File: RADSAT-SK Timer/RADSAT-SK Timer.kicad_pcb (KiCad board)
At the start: 2 copper layers, 90.2 x 95.9 mm, 122 parts, among them J101 Conn_02x26_Odd_Even, J103 Conn_02x26_Odd_Even, J201 Conn_01x07, J202 Conn_01x05, J203 Conn_01x03, J204 Conn_01x02, J205 Conn_01x02, J206 Conn_01x02, J210 ZX62WRD-B-5PC, Q101 IRLML2060, Q102 IRLML2060, Q103 IRLML2060, Q104 IRLML2060, Q105 IRLML2060, Q106 IRLML2060, Q107 IRLML2060, Q108 IRLML2060, Q109 IRLML2060, Q201 IRLML2060, Q202 IRLML2060, Q204 IRLML2060, Q205 IRLML2060, Q206 IRLML2060, SW201 SW_Push, SW202 SW_Push, SW203 SW_Push, SW204 SW_Push, SW205 SW_Push, SW206 SW_Push, U101 LM397MF, U102 LM397MF, U103 LM397MF, U104 CD4052B, U202 LTC3440EMSPBF, U230 CPC1117N, U240 CPC1117N, U250 CPC1117N, U260 CPC1117N

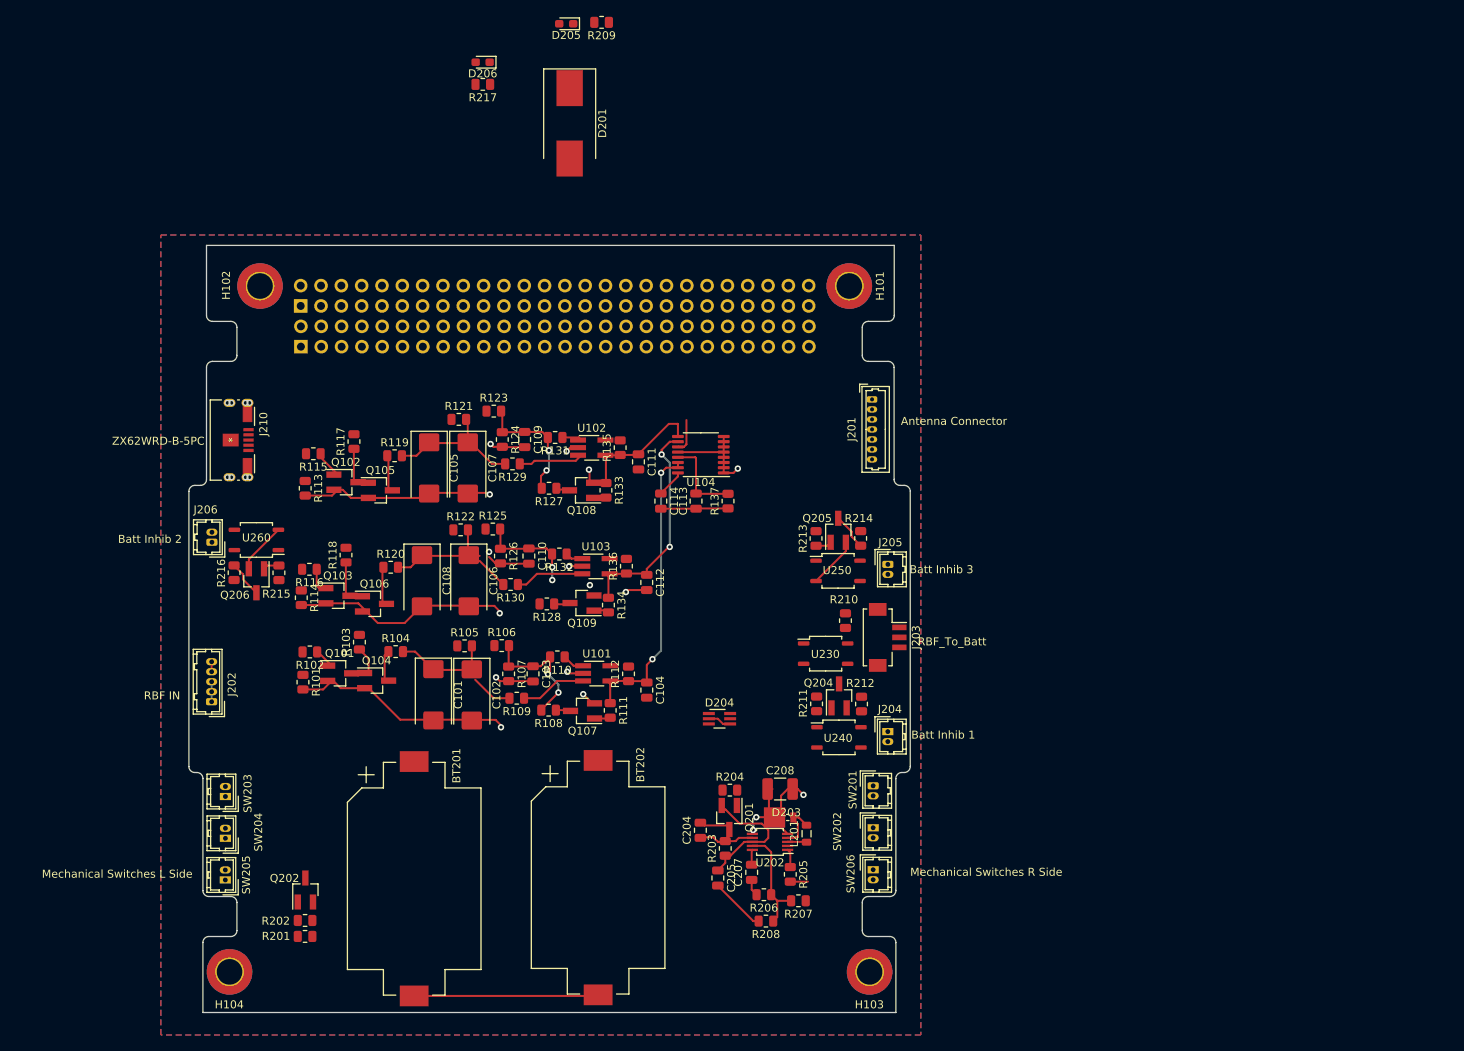
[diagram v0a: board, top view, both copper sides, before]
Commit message: better layour for timer components
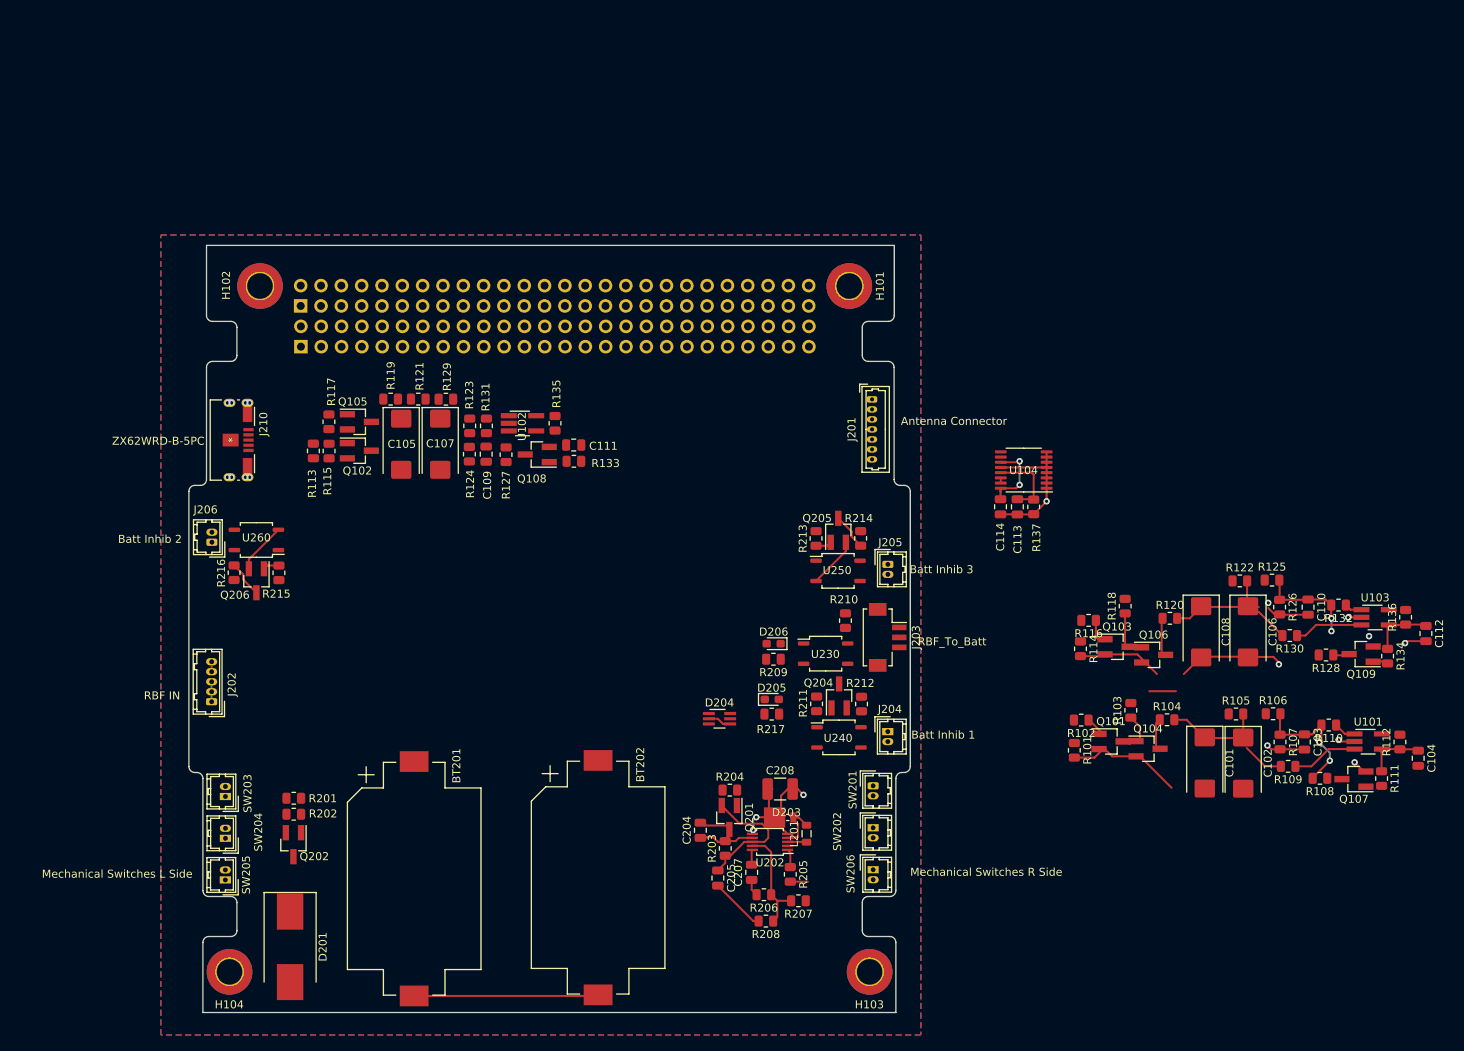
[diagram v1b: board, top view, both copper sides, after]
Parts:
- moved D201 108.7 mm to (47.5, 137.7)
- moved C108 97.6 mm to (161.4, 98.3)
- moved R120 97.6 mm to (157.5, 96.6)
- moved R122 97.6 mm to (166.2, 91.9)
- moved R134 97.6 mm to (184.7, 101.3)
- moved R136 97.6 mm to (186.9, 96.5)
- moved U103 97.6 mm to (183.1, 96.5)
- moved C106 97.6 mm to (167.2, 98.3)
- moved C110 97.6 mm to (174.7, 95.2)
- moved C112 97.6 mm to (189.5, 98.5)
- moved Q103 97.6 mm to (150.8, 100.2)
- moved Q106 97.6 mm to (155.4, 101.2)
- moved R114 97.6 mm to (146.3, 100.4)
- moved R126 97.6 mm to (171.2, 95.2)
- moved R130 97.6 mm to (172.4, 98.8)
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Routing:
- net GND: track 147.7 -> 100.2 mm, vias 15 -> 10
- net Timer_A_out: track 37.9 -> 8.59 mm, vias 2 -> 0
- net Timer_C_out: track 28.0 -> 8.28 mm, vias 2 -> 0
- net Net-(C105-Pad1): track 17.2 -> 0.00 mm
- net Timer_B_out: track 16.3 -> 0.00 mm
- net Net-(C109-Pad1): track 15.4 -> 0.00 mm, vias 2 -> 0
- net Net-(R129-Pad1): track 8.13 -> 0.00 mm
- net Net-(Q102-Pad3): track 6.52 -> 0.09 mm
- net Net-(Q105-Pad3): track 4.37 -> 0.00 mm
- net Net-(Q102-Pad1): track 3.50 -> 0.00 mm
- net Net-(Q107-Pad1): track 2.50 -> 0.00 mm
- net Net-(R131-Pad1): track 2.48 -> 0.00 mm
- net Net-(Q107-Pad3): track 2.37 -> 0.00 mm
- net Net-(Q108-Pad3): track 2.26 -> 0.00 mm
- net Net-(Q108-Pad1): track 2.06 -> 0.00 mm
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
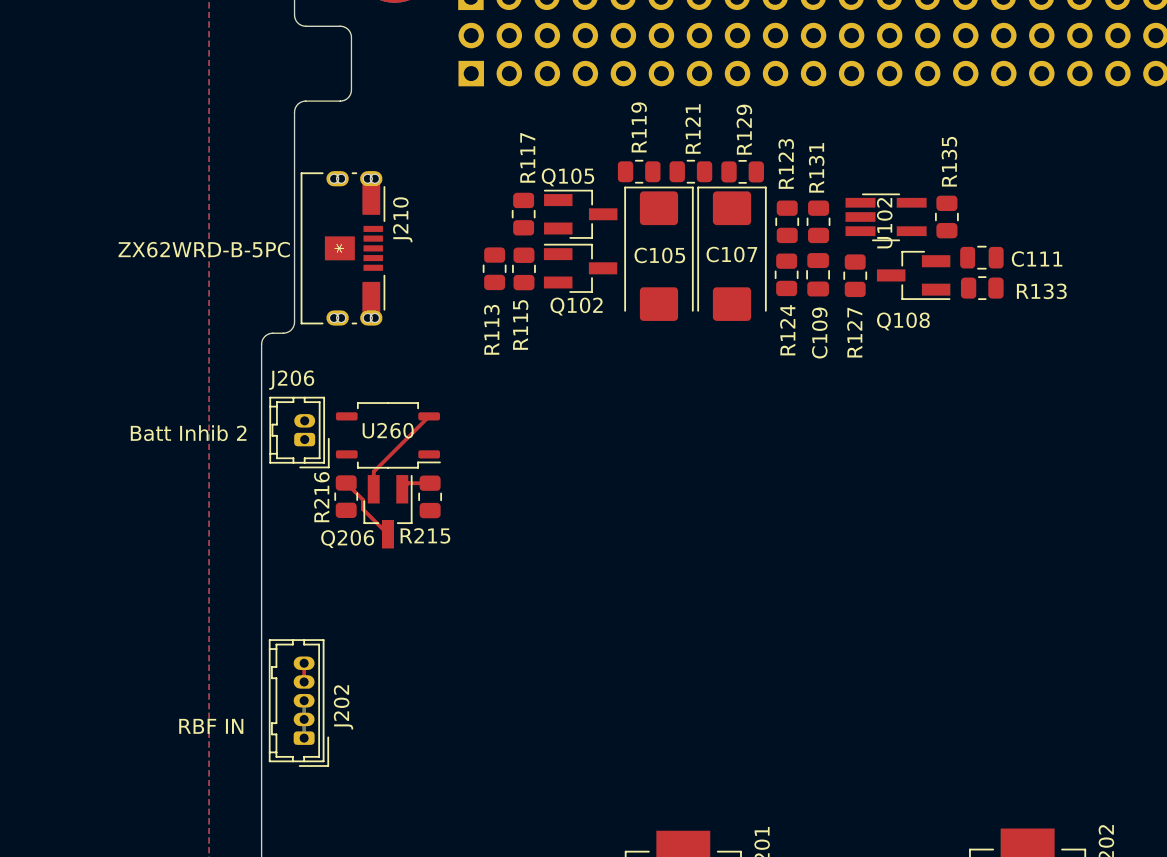
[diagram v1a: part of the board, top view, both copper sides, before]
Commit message: Made changes to accomadate the RBF alternate charge plug
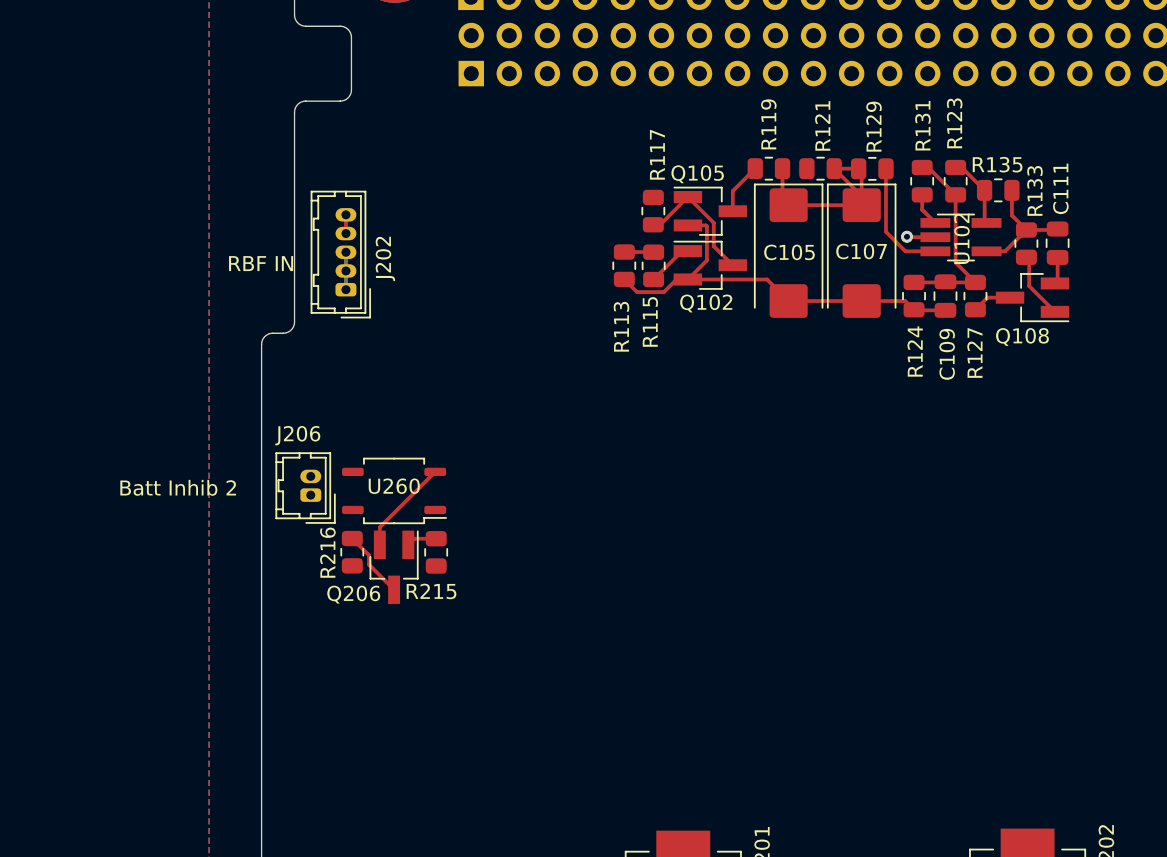
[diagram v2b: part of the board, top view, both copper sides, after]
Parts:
- removed J210: ZX62WRD-B-5PC, CONN_ZX62WRD-B-5PC_HIR:CONN_ZX62WRD-B-5PC_HIR
- moved J202 30.1 mm to (40.5, 77.1)
- moved R123 11.6 mm to (81.2, 69.8)
- moved C105 8.66 mm to (70.0, 74.7)
- moved C107 8.66 mm to (74.9, 74.7)
- moved Q102 8.66 mm to (64.8, 75.5)
- moved Q105 8.66 mm to (64.8, 71.9)
- moved R113 8.66 mm to (59.0, 75.5)
- moved R115 8.66 mm to (61.0, 75.5)
- moved R117 8.66 mm to (61.0, 71.8)
- moved R119 8.66 mm to (68.7, 69.0)
- moved R121 8.66 mm to (72.2, 69.0)
- moved R129 8.66 mm to (75.6, 69.0)
- moved C109 8.62 mm to (80.5, 77.5)
- moved R124 8.62 mm to (78.4, 77.5)
- moved R127 8.14 mm to (82.5, 77.5)
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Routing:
- net GND: track 100.2 -> 132.3 mm, vias 10 -> 11
- net Net-(C105-Pad1): track 0.00 -> 14.8 mm
- net Net-(C109-Pad1): track 0.00 -> 13.5 mm
- net Net-(Q102-Pad3): track 0.09 -> 8.97 mm
- net Timer_B_out: track 0.00 -> 8.40 mm
- net Net-(R129-Pad1): track 0.00 -> 8.04 mm
- net +BATT: track 17.1 -> 23.9 mm
- net Net-(Q108-Pad1): track 0.00 -> 4.43 mm
- net Net-(Q105-Pad3): track 0.00 -> 3.46 mm
- net Net-(Q102-Pad1): track 0.00 -> 3.07 mm
- net Net-(Q108-Pad3): track 0.00 -> 2.65 mm
- net Net-(R131-Pad1): track 0.00 -> 2.24 mm

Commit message: single wire was missing, final commit before merging to main
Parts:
- moved R201 2.33 mm to (47.1, 117.0)
- moved R202 1.96 mm to (47.1, 119.4)

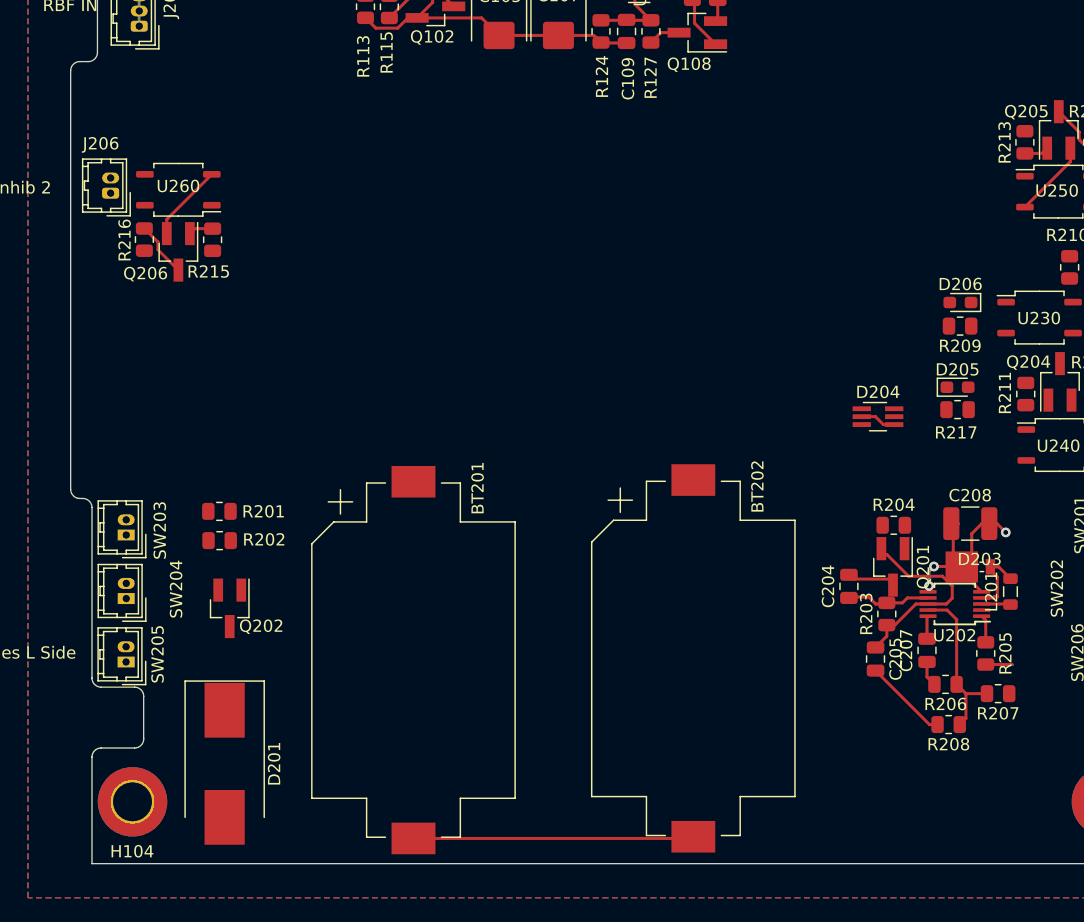
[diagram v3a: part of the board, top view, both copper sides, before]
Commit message: RBF Circuit was modified and new components added to BOM
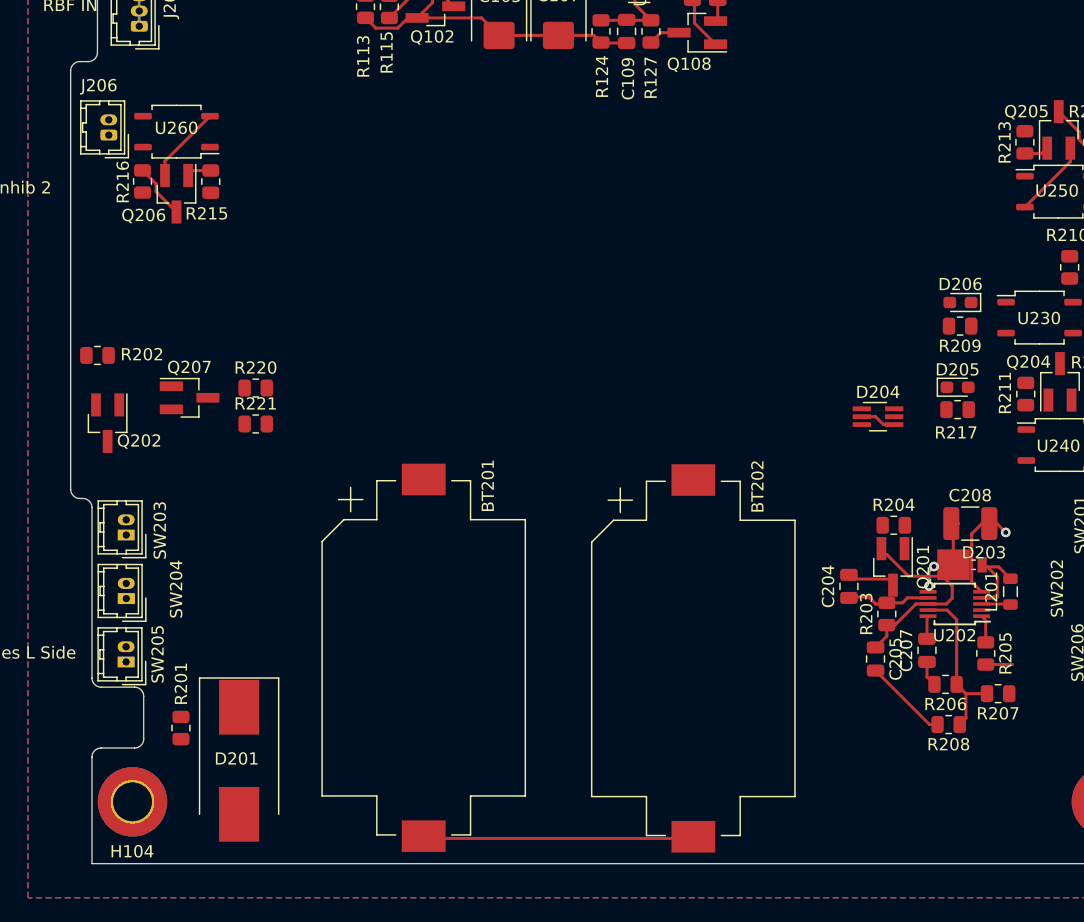
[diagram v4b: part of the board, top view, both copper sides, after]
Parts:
- added Q207: IRLML2060, Package_TO_SOT_SMD:SOT-23_Handsoldering, F.Cu at (44.6, 107.6)
- added R220: 100, Resistor_SMD:R_0805_2012Metric, F.Cu at (50.0, 106.8)
- added R221: 1M, Resistor_SMD:R_0805_2012Metric, F.Cu at (50.0, 109.8)
- moved R202 18.2 mm to (37.0, 104.1)
- moved Q202 18.2 mm to (37.9, 109.7)
- moved R201 18.1 mm to (43.9, 134.7), turned to 270 degrees
- moved J206 4.78 mm to (38.0, 86.0)
- moved Q206 4.78 mm to (43.5, 90.9)
- moved R215 4.78 mm to (46.3, 89.9)
- moved R216 4.78 mm to (40.7, 89.8)
- moved U260 4.78 mm to (43.5, 85.8)
- moved D201 1.21 mm to (48.7, 137.4)
- moved BT201 0.86 mm to (63.8, 129.0)
- moved D203 0.70 mm to (108.1, 121.3)
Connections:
- J101 pad 14: GND -> (no net)
- J101 pad 25: (no net) -> +5V
- J101 pad 27: (no net) -> +3V3
- J101 pad 29: (no net) -> GND
- J101 pad 30: (no net) -> GND
- J101 pad 32: (no net) -> GND
- J202 pad 1: Net-(D201-Pad1) -> Net-(BT201-Pad1)
- J202 pad 3: Net-(D201-Pad1) -> USB_Charge
- J202 pad 4: Net-(BT201-Pad1) -> GND
- J202 pad 5: Net-(BT201-Pad1) -> (no net)
- R202 pad 2: Net-(D201-Pad1) -> Net-(Q207-Pad3)
- SW203 pad 2: Net-(SW201-Pad1) -> Net-(SW203-Pad2)
- SW204 pad 2: Net-(SW201-Pad1) -> Net-(SW203-Pad2)
